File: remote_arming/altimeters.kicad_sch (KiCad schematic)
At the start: 34 parts, among them J10 Drogue Pyro, J6 A2 Connector, J7 A1 Connector, J8 SL Data Connector, J9 Main Pyros, Q1 DMG2302UK, Q2 DMG2302UK, Q3 AOD417, Q4 AOD417, Q5 BSS138

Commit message: changed 5v pull up resistors to BATT pwr with voltage divider
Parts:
- R11, R12: value 10k -> 1.4k
- R24, R25: value DNP -> 700R
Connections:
- net +5V: no longer R11.1, R12.1
- net +BATT: now also R11.1, R12.1
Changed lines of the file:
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@@
       (effects (font (size 1.27 1.27)) (justify left))
     )
-    (property "Value" "10k" (at 47.4472 60.833 0)
+    (property "Value" "1.4k" (at 47.4472 60.833 0)
       (effects (font (size 1.27 1.27)) (justify left))
     )
@@
     )
   )
-  (symbol (lib_id "power:+5V") (at 45.72 55.88 0) (unit 1)
-    (in_bom yes) (on_board yes) (dnp no)
-    (property "Reference" "#PWR029" (at 45.72 59.69 0)
-      (effects (font (size 1.27 1.27)) hide)
-    )
-    (property "Value" "+5V" (at 46.101 51.4858 0)
-      (effects (font (size 1.27 1.27)))
-    )
-    (property "Footprint" "" (at 45.72 55.88 0)
-      (effects (font (size 1.27 1.27)) hide)
-    )
-    (property "Datasheet" "" (at 45.72 55.88 0)
-      (effects (font (size 1.27 1.27)) hide)
-    )
-    (pin "1")
-    (instances
-      (project "remote_arming"
-        (path "/66ac2ba2-aeaf-4c0b-bff0-9252049e25ae/00000000-0000-0000-0000-00005da13d99"
-          (reference "#PWR029") (unit 1)
-        )
-      )
-    )
-  )
   (symbol (lib_id "Device:Q_PMOS_GDS") (at 92.71 143.51 0) (mirror x) (unit 1)
     (in_bom yes) (on_board yes) (dnp no)
@@
       (effects (font (size 1.27 1.27)) (justify left))
     )
-    (property "Value" "10k" (at 46.1772 153.543 0)
+    (property "Value" "1.4k" (at 46.1772 153.543 0)
       (effects (font (size 1.27 1.27)) (justify left))
     )
@@
         (path "/66ac2ba2-aeaf-4c0b-bff0-9252049e25ae/00000000-0000-0000-0000-00005da13d99"
           (reference "R11") (unit 1)
-        )
-      )
-    )
-  )
-  (symbol (lib_id "power:+5V") (at 44.45 148.59 0) (unit 1)
-    (in_bom yes) (on_board yes) (dnp no)
-    (property "Reference" "#PWR028" (at 44.45 152.4 0)
-      (effects (font (size 1.27 1.27)) hide)
-    )
-    (property "Value" "+5V" (at 44.831 144.1958 0)
-      (effects (font (size 1.27 1.27)))
-    )
-    (property "Footprint" "" (at 44.45 148.59 0)
-      (effects (font (size 1.27 1.27)) hide)
-    )
-    (property "Datasheet" "" (at 44.45 148.59 0)
-      (effects (font (size 1.27 1.27)) hide)
-    )
-    (pin "1")
-    (instances
-      (project "remote_arming"
-        (path "/66ac2ba2-aeaf-4c0b-bff0-9252049e25ae/00000000-0000-0000-0000-00005da13d99"
-          (reference "#PWR028") (unit 1)
         )
       )
@@
       (effects (font (size 1.27 1.27)) (justify left))
     )
-    (property "Value" "DNP" (at 47.4472 77.343 0)
+    (property "Value" "700R" (at 47.4472 77.343 0)
       (effects (font (size 1.27 1.27)) (justify left))
     )
@@
       (effects (font (size 1.27 1.27)) (justify left))
     )
-    (property "Value" "DNP" (at 46.1772 168.783 0)
+    (property "Value" "700R" (at 46.1772 168.783 0)
       (effects (font (size 1.27 1.27)) (justify left))
     )
@@
     )
   )
+  (symbol (lib_name "+BATT_2") (lib_id "power:+BATT") (at 44.45 148.59 0) (unit 1)
+    (in_bom yes) (on_board yes) (dnp no) (fields_autoplaced)
+    (property "Reference" "#PWR053" (at 44.45 152.4 0)
+      (effects (font (size 1.27 1.27)) hide)
+    )
+    (property "Value" "+BATT2" (at 44.45 143.51 0)
+      (effects (font (size 1.27 1.27)))
+    )
+    (property "Footprint" "" (at 44.45 148.59 0)
+      (effects (font (size 1.27 1.27)) hide)
+    )
+    (property "Datasheet" "" (at 44.45 148.59 0)
+      (effects (font (size 1.27 1.27)) hide)
+    )
+    (pin "1")
+    (instances
+      (project "remote_arming"
+        (path "/66ac2ba2-aeaf-4c0b-bff0-9252049e25ae/00000000-0000-0000-0000-00005da13c95"
+          (reference "#PWR053") (unit 1)
+        )
+        (path "/66ac2ba2-aeaf-4c0b-bff0-9252049e25ae/00000000-0000-0000-0000-00005da13d99"
+          (reference "#PWR028") (unit 1)
+        )
+      )
+    )
+  )
   (symbol (lib_name "+BATT_1") (lib_id "power:+BATT") (at 95.25 38.1 0) (unit 1)
     (in_bom yes) (on_board yes) (dnp no) (fields_autoplaced)
@@
         )
       )
+    )
+  )
+  (symbol (lib_name "+BATT_1") (lib_id "power:+BATT") (at 45.72 55.88 0) (unit 1)
+    (in_bom yes) (on_board yes) (dnp no) (fields_autoplaced)
+    (property "Reference" "#PWR018" (at 45.72 59.69 0)
+      (effects (font (size 1.27 1.27)) hide)
+    )
+    (property "Value" "+BATT1" (at 45.72 50.8 0)
+      (effects (font (size 1.27 1.27)))
+    )
+    (property "Footprint" "" (at 45.72 55.88 0)
+      (effects (font (size 1.27 1.27)) hide)
+    )
+    (property "Datasheet" "" (at 45.72 55.88 0)
+      (effects (font (size 1.27 1.27)) hide)
+    )
+    (pin "1")
+    (instances
+      (project "remote_arming"
+        (path "/66ac2ba2-aeaf-4c0b-bff0-9252049e25ae/00000000-0000-0000-0000-00005da13c95"
+          (reference "#PWR018") (unit 1)
+        )
+        (path "/66ac2ba2-aeaf-4c0b-bff0-9252049e25ae/00000000-0000-0000-0000-00005da13d99"
+          (reference "#PWR029") (unit 1)
+        )
+      )

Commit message: changed Main/Drogue connectors to Altimeter1/Altimeter2
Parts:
- J10: value Drogue Pyro -> A2 Connections
- J9: value Main Pyros -> A1 Connections
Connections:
- net D2+: now also J9.6 (Pin_6); no longer J10.6 (Pin_6)
- net D2_PYRO: now also J9.4 (Pin_4); no longer J10.4 (Pin_4)
- net M2+: now also J10.6 (Pin_6); no longer J9.6 (Pin_6)
- net M2_PYRO: now also J10.4 (Pin_4); no longer J9.4 (Pin_4)
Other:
- moved on the sheet: J6, J7, R19, R20, R21, R22

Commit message: batt supplies 9v not 15v :p, fixed voltage divider values
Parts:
- R11, R12: value 1.4k -> 200R
- R24, R25: value 700R -> 250R
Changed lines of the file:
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@@
       (effects (font (size 1.27 1.27)) (justify left))
     )
-    (property "Value" "1.4k" (at 47.4472 60.833 0)
+    (property "Value" "200R" (at 47.4472 60.833 0)
       (effects (font (size 1.27 1.27)) (justify left))
     )
@@
       (effects (font (size 1.27 1.27)) (justify left))
     )
-    (property "Value" "1.4k" (at 46.1772 153.543 0)
+    (property "Value" "200R" (at 46.1772 153.543 0)
       (effects (font (size 1.27 1.27)) (justify left))
     )
@@
       (effects (font (size 1.27 1.27)) (justify left))
     )
-    (property "Value" "700R" (at 47.4472 77.343 0)
+    (property "Value" "250R" (at 47.4472 77.343 0)
       (effects (font (size 1.27 1.27)) (justify left))
     )
@@
       (effects (font (size 1.27 1.27)) (justify left))
     )
-    (property "Value" "700R" (at 46.1772 168.783 0)
-      (effects (font (size 1.27 1.27)) (justify left))
-    )
+    (property "Value" "250R" (at 46.1772 168.783 0)
+      (effects (font (size 1.27 1.27)) (justify left))
+    )

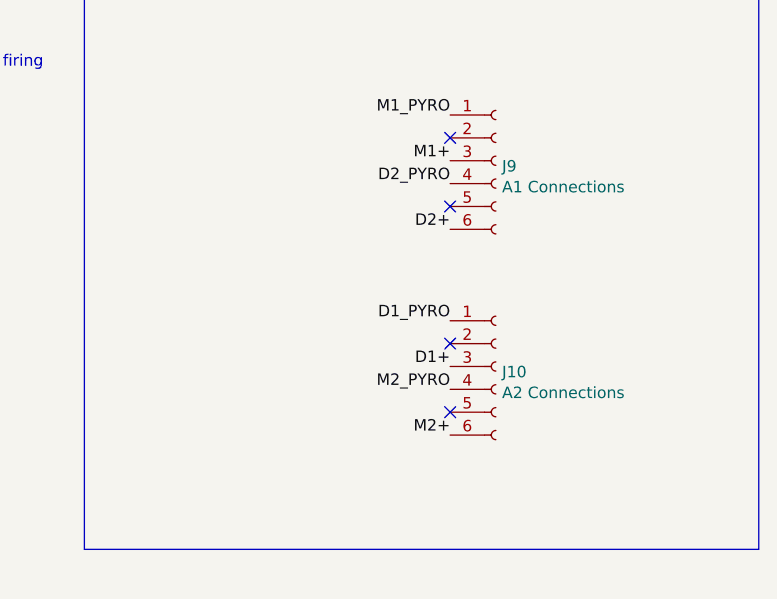
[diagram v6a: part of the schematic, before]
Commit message: fixed inconsistent altimeter outputs
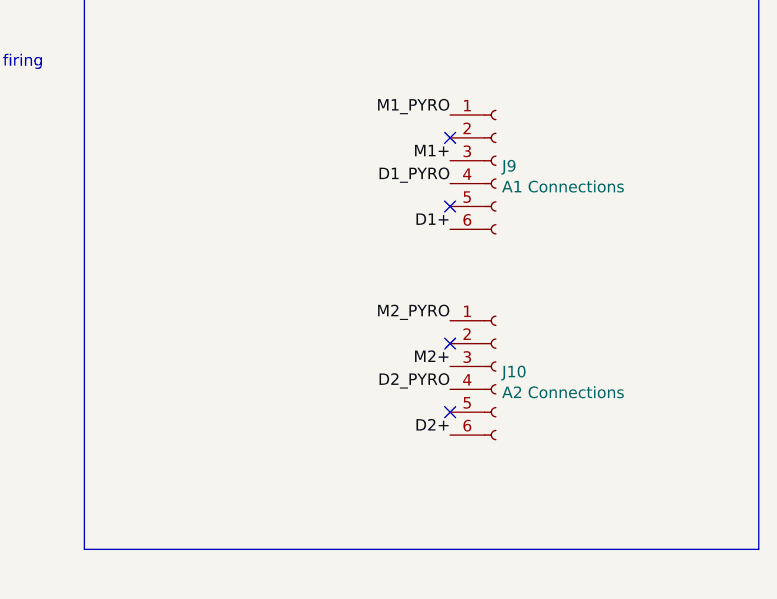
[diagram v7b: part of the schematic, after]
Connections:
- net D1+: now also J9.6 (Pin_6); no longer J10.3 (Pin_3)
- net D1_PYRO: now also J9.4 (Pin_4); no longer J10.1 (Pin_1)
- net D2+: now also J10.6 (Pin_6); no longer J9.6 (Pin_6)
- net D2_PYRO: now also J10.4 (Pin_4); no longer J9.4 (Pin_4)
- net M2+: now also J10.3 (Pin_3); no longer J10.6 (Pin_6)
- net M2_PYRO: now also J10.1 (Pin_1); no longer J10.4 (Pin_4)
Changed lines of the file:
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@@
     (effects (font (size 1.27 1.27)) (justify left bottom))
   )
-  (label "M2+" (at 247.65 149.86 180) (fields_autoplaced)
+  (label "M2+" (at 247.65 142.24 180) (fields_autoplaced)
     (effects (font (size 1.27 1.27)) (justify right bottom))
   )
@@
     (effects (font (size 1.27 1.27)) (justify left bottom))
   )
-  (label "D1+" (at 247.65 142.24 180) (fields_autoplaced)
+  (label "D1+" (at 247.65 127 180) (fields_autoplaced)
     (effects (font (size 1.27 1.27)) (justify right bottom))
   )
-  (label "D2+" (at 247.65 127 180) (fields_autoplaced)
+  (label "D2+" (at 247.65 149.86 180) (fields_autoplaced)
     (effects (font (size 1.27 1.27)) (justify right bottom))
   )
@@
     (effects (font (size 1.27 1.27)) (justify right bottom))
   )
-  (label "D1_PYRO" (at 247.65 137.16 180) (fields_autoplaced)
+  (label "D1_PYRO" (at 247.65 121.92 180) (fields_autoplaced)
     (effects (font (size 1.27 1.27)) (justify right bottom))
   )
@@
     (effects (font (size 1.27 1.27)) (justify left bottom))
   )
-  (label "D2_PYRO" (at 247.65 121.92 180) (fields_autoplaced)
+  (label "D2_PYRO" (at 247.65 144.78 180) (fields_autoplaced)
     (effects (font (size 1.27 1.27)) (justify right bottom))
   )
@@
     (effects (font (size 1.27 1.27)) (justify right bottom))
   )
-  (label "M2_PYRO" (at 247.65 144.78 180) (fields_autoplaced)
+  (label "M2_PYRO" (at 247.65 137.16 180) (fields_autoplaced)
     (effects (font (size 1.27 1.27)) (justify right bottom))
   )
